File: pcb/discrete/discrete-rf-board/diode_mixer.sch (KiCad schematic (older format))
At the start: 27 parts, among them J301 Conn_Coaxial, J302 Conn_Coaxial, U302 BAT15-099R

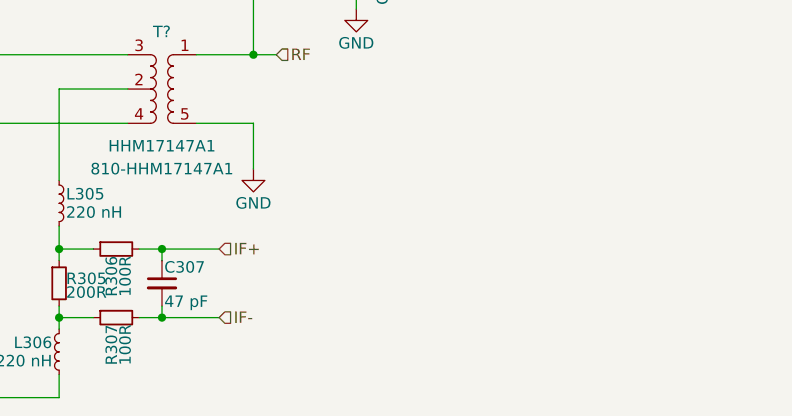
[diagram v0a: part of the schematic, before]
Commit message: Design DAC/ADC stages, pass out all control signals to top sheet
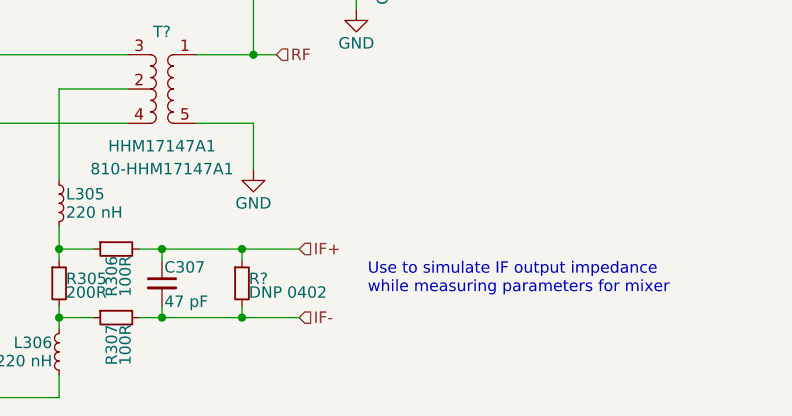
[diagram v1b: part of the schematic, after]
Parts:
- added R?: DNP 0402, symbol Device:R_Small
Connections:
- net IF+: now also R?.1
- net IF-: now also R?.2
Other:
- note added: "Use to simulate IF output impedance\nwhile measuring parameters for mixer"
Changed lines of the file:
@@
 RF
 Wire Wire Line
-	9000 4300 8750 4300
+	9350 4300 9100 4300
 Connection ~ 8750 4300
 Wire Wire Line
@@
 	8750 4600 8750 4550
 Wire Wire Line
-	9000 4600 8750 4600
+	9350 4600 9100 4600
 Connection ~ 8750 4600
-Text HLabel 9000 4300 2    50   Input ~ 0
+Text HLabel 9350 4300 2    50   Input ~ 0
 IF+
-Text HLabel 9000 4600 2    50   Input ~ 0
+Text HLabel 9350 4600 2    50   Input ~ 0
 IF-
 Wire Wire Line
@@
 Text Notes 4850 4350 0    50   ~ 0
 TODO probably add bypass cap, probably ground some part of\nthe balanced mixer to make TL design easier
+$Comp
+L Device:R_Small R?
+U 1 1 5D979A64
+P 9100 4450
+AR Path="/5CA6B0AA/5CC1CC09/5D979A64" Ref="R?"  Part="1"
+AR Path="/5CA6B0AA/5CC4015A/5D979A64" Ref="R?"  Part="1"
+F 0 "R?" H 9130 4470 50  0000 L CNN
+F 1 "DNP 0402" H 9130 4410 50  0000 L CNN
+F 2 "" H 9100 4450 50  0001 C CNN
+F 3 "~" H 9100 4450 50  0001 C CNN
+	1    9100 4450
+	1    0    0    -1
+$EndComp
+Text Notes 9650 4500 0    50   ~ 0
+Use to simulate IF output impedance\nwhile measuring parameters for mixer
+Wire Wire Line
+	9100 4350 9100 4300
+Connection ~ 9100 4300
+Wire Wire Line
+	9100 4300 8750 4300
+Wire Wire Line
+	9100 4550 9100 4600
+Connection ~ 9100 4600
+Wire Wire Line
+	9100 4600 8750 4600
 $EndSCHEMATC

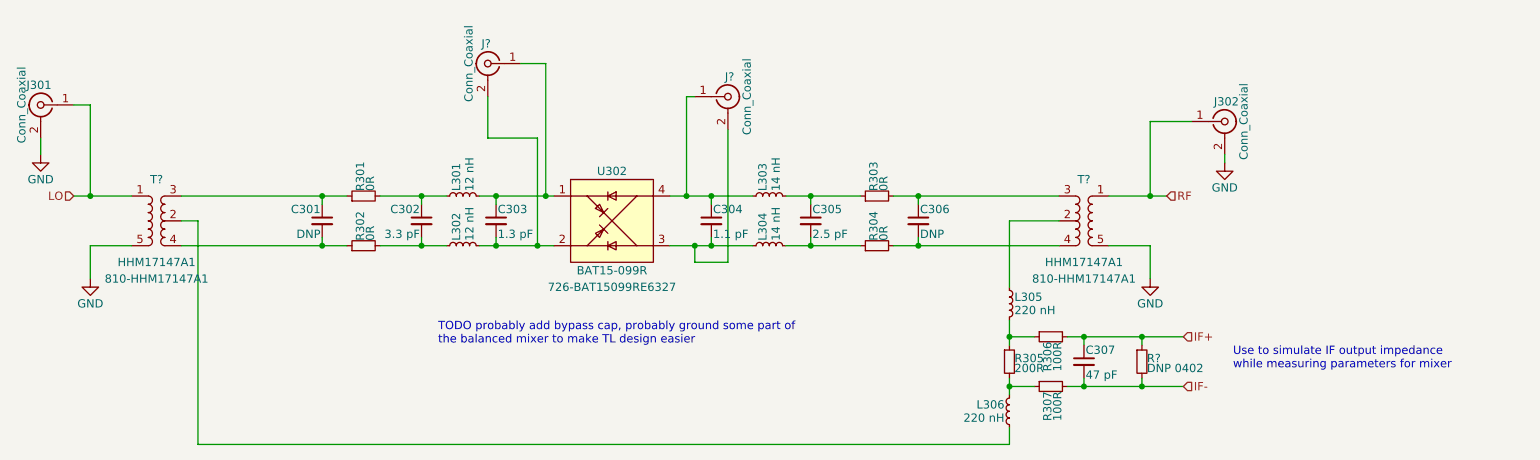
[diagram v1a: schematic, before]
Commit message: Wire out all control signals to connectors TODO PLL charge pump loop, bypass caps in attenuator circuit, antialiasing filter for ADC frontend
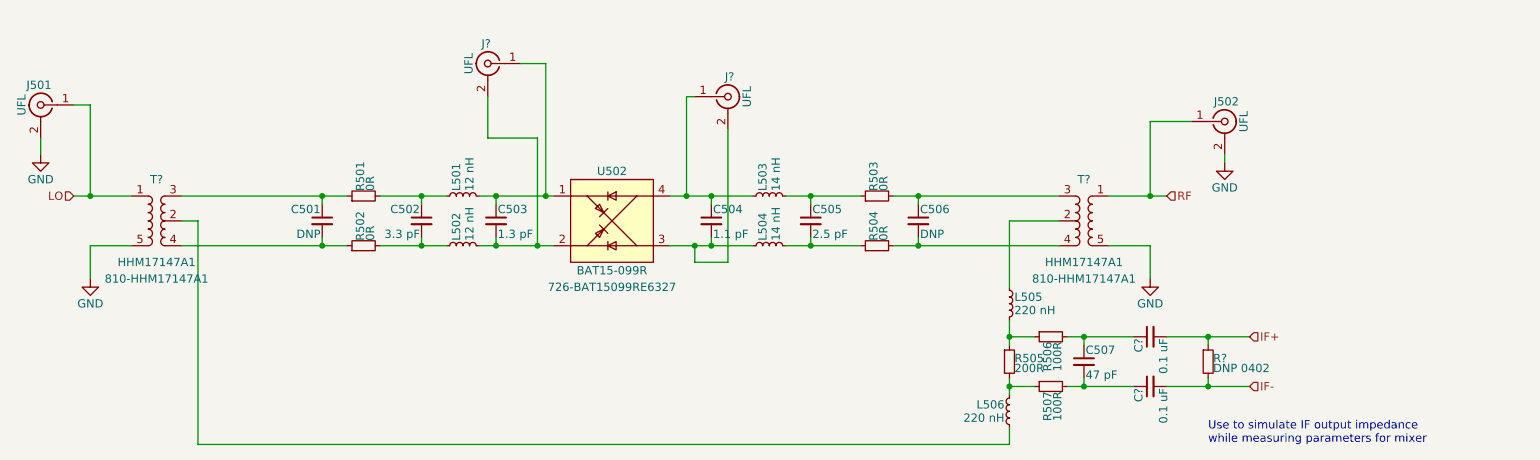
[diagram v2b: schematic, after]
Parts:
- added C? (x2): 0.1 uF, symbol Device:C_Small
- J301, J302, J? (x2): value Conn_Coaxial -> UFL
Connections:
- net IF+: now also C?.2; no longer C307.1, R306.2
- net IF-: now also C?.2; no longer C307.2, R307.2
- new net: C307.1, C?.1, R306.2
- new net: C307.2, C?.1, R307.2
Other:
- note removed: "TODO probably add bypass cap, probably ground some part of\nthe balanced mixer to make TL design easier"
- moved on the sheet: R?

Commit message: Start work in footprinting everything
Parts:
- U302: footprint (none) -> discrete_footprints:Infineon_SOT143
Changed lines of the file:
@@
 $Descr A4 11693 8268
 encoding utf-8
-Sheet 19 19
+Sheet 11 19
 Title ""
 Date ""
@@
 F 0 "U502" H 5900 3900 50  0000 C CNN
 F 1 "BAT15-099R" H 5900 3300 50  0000 C CNN
-F 2 "" H 5900 3900 50  0001 C CNN
+F 2 "discrete_footprints:Infineon_SOT143" H 5900 3900 50  0001 C CNN
 F 3 "" H 5900 3900 50  0001 C CNN
 F 4 "726-BAT15099RE6327" H 5900 3200 50  0000 C CNN "Mouser"

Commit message: The footprintening continues
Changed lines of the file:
@@
 $Descr A4 11693 8268
 encoding utf-8
-Sheet 11 19
+Sheet 19 19
 Title ""
 Date ""
@@
 AR Path="/5CA6B0AA/5CC1CC09/5CC1E322" Ref="U302"  Part="1"
 AR Path="/5CA6B0AA/5CC4015A/5CC1E322" Ref="U502"  Part="1"
-F 0 "U502" H 5900 3900 50  0000 C CNN
+F 0 "U302" H 5900 3900 50  0000 C CNN
 F 1 "BAT15-099R" H 5900 3300 50  0000 C CNN
 F 2 "discrete_footprints:Infineon_SOT143" H 5900 3900 50  0001 C CNN
@@
 AR Path="/5CA6B0AA/5CC1CC09/5CC1F89D" Ref="C304"  Part="1"
 AR Path="/5CA6B0AA/5CC4015A/5CC1F89D" Ref="C504"  Part="1"
-F 0 "C504" H 6510 3670 50  0000 L CNN
+F 0 "C304" H 6510 3670 50  0000 L CNN
 F 1 "1.1 pF" H 6510 3520 50  0000 L CNN
 F 2 "" H 6500 3600 50  0001 C CNN
@@
 AR Path="/5CA6B0AA/5CC1CC09/5CC20238" Ref="C305"  Part="1"
 AR Path="/5CA6B0AA/5CC4015A/5CC20238" Ref="C505"  Part="1"
-F 0 "C505" H 7110 3670 50  0000 L CNN
+F 0 "C305" H 7110 3670 50  0000 L CNN
 F 1 "2.5 pF" H 7110 3520 50  0000 L CNN
 F 2 "" H 7100 3600 50  0001 C CNN
@@
 AR Path="/5CA6B0AA/5CC1CC09/5CC208EE" Ref="L304"  Part="1"
 AR Path="/5CA6B0AA/5CC4015A/5CC208EE" Ref="L504"  Part="1"
-F 0 "L504" H 6880 3790 50  0000 L CNN
+F 0 "L304" H 6880 3790 50  0000 L CNN
 F 1 "14 nH" H 6880 3710 50  0000 L CNN
 F 2 "" H 6850 3750 50  0001 C CNN
@@
 AR Path="/5CA6B0AA/5CC1CC09/5CC2101C" Ref="L303"  Part="1"
 AR Path="/5CA6B0AA/5CC4015A/5CC2101C" Ref="L503"  Part="1"
-F 0 "L503" H 6880 3490 50  0000 L CNN
+F 0 "L303" H 6880 3490 50  0000 L CNN
 F 1 "14 nH" H 6880 3410 50  0000 L CNN
 F 2 "" H 6850 3450 50  0001 C CNN
@@
 AR Path="/5CA6B0AA/5CC1CC09/5CC289D9" Ref="L305"  Part="1"
 AR Path="/5CA6B0AA/5CC4015A/5CC289D9" Ref="L505"  Part="1"
-F 0 "L505" H 8330 4140 50  0000 L CNN
+F 0 "L305" H 8330 4140 50  0000 L CNN
 F 1 "220 nH" H 8330 4060 50  0000 L CNN
 F 2 "" H 8300 4100 50  0001 C CNN
@@
 AR Path="/5CA6B0AA/5CC1CC09/5CC29B4E" Ref="R305"  Part="1"
 AR Path="/5CA6B0AA/5CC4015A/5CC29B4E" Ref="R505"  Part="1"
-F 0 "R505" H 8330 4470 50  0000 L CNN
+F 0 "R305" H 8330 4470 50  0000 L CNN
 F 1 "200R" H 8330 4410 50  0000 L CNN
 F 2 "" H 8300 4450 50  0001 C CNN
@@
 AR Path="/5CA6B0AA/5CC1CC09/5CC29F9D" Ref="R306"  Part="1"
 AR Path="/5CA6B0AA/5CC4015A/5CC29F9D" Ref="R506"  Part="1"
-F 0 "R506" H 8580 4320 50  0000 L CNN
+F 0 "R306" H 8580 4320 50  0000 L CNN
 F 1 "100R" H 8580 4260 50  0000 L CNN
 F 2 "" H 8550 4300 50  0001 C CNN
@@
 AR Path="/5CA6B0AA/5CC1CC09/5CC2B0AC" Ref="C307"  Part="1"
 AR Path="/5CA6B0AA/5CC4015A/5CC2B0AC" Ref="C507"  Part="1"
-F 0 "C507" H 8760 4520 50  0000 L CNN
+F 0 "C307" H 8760 4520 50  0000 L CNN
 F 1 "47 pF" H 8760 4370 50  0000 L CNN
 F 2 "" H 8750 4450 50  0001 C CNN
@@
 AR Path="/5CA6B0AA/5CC1CC09/5CC2FA5E" Ref="#PWR0302"  Part="1"
 AR Path="/5CA6B0AA/5CC4015A/5CC2FA5E" Ref="#PWR0502"  Part="1"
-F 0 "#PWR0502" H 2750 3700 50  0001 C CNN
+F 0 "#PWR0302" H 2750 3700 50  0001 C CNN
 F 1 "GND" H 2750 3800 50  0000 C CNN
 F 2 "" H 2750 3950 50  0001 C CNN
@@
 AR Path="/5CA6B0AA/5CC1CC09/5CC3011D" Ref="#PWR0303"  Part="1"
 AR Path="/5CA6B0AA/5CC4015A/5CC3011D" Ref="#PWR0503"  Part="1"
-F 0 "#PWR0503" H 9150 3700 50  0001 C CNN
+F 0 "#PWR0303" H 9150 3700 50  0001 C CNN
 F 1 "GND" H 9150 3800 50  0000 C CNN
 F 2 "" H 9150 3950 50  0001 C CNN
@@
 AR Path="/5CA6B0AA/5CC1CC09/5CC30B27" Ref="J301"  Part="1"
 AR Path="/5CA6B0AA/5CC4015A/5CC30B27" Ref="J501"  Part="1"
-F 0 "J501" H 2460 3020 50  0000 C CNN
+F 0 "J301" H 2460 3020 50  0000 C CNN
 F 1 "UFL" V 2565 2900 50  0000 C CNN
 F 2 "" H 2450 2900 50  0001 C CNN
@@
 AR Path="/5CA6B0AA/5CC1CC09/5CC31787" Ref="J302"  Part="1"
 AR Path="/5CA6B0AA/5CC4015A/5CC31787" Ref="J502"  Part="1"
-F 0 "J502" H 9610 3120 50  0000 C CNN
+F 0 "J302" H 9610 3120 50  0000 C CNN
 F 1 "UFL" V 9715 3000 50  0000 C CNN
 F 2 "" H 9600 3000 50  0001 C CNN
@@
 AR Path="/5CA6B0AA/5CC1CC09/5CC33186" Ref="#PWR0304"  Part="1"
 AR Path="/5CA6B0AA/5CC4015A/5CC33186" Ref="#PWR0504"  Part="1"
-F 0 "#PWR0504" H 9600 3000 50  0001 C CNN
+F 0 "#PWR0304" H 9600 3000 50  0001 C CNN
 F 1 "GND" H 9600 3100 50  0000 C CNN
 F 2 "" H 9600 3250 50  0001 C CNN
@@
 AR Path="/5CA6B0AA/5CC1CC09/5CC33A73" Ref="#PWR0301"  Part="1"
 AR Path="/5CA6B0AA/5CC4015A/5CC33A73" Ref="#PWR0501"  Part="1"
-F 0 "#PWR0501" H 2450 2950 50  0001 C CNN
+F 0 "#PWR0301" H 2450 2950 50  0001 C CNN
 F 1 "GND" H 2450 3050 50  0000 C CNN
 F 2 "" H 2450 3200 50  0001 C CNN
@@
 AR Path="/5CA6B0AA/5CC1CC09/5CC5AE0B" Ref="L306"  Part="1"
 AR Path="/5CA6B0AA/5CC4015A/5CC5AE0B" Ref="L506"  Part="1"
-F 0 "L506" H 8330 4790 50  0000 L CNN
+F 0 "L306" H 8330 4790 50  0000 L CNN
 F 1 "220 nH" H 8330 4710 50  0000 L CNN
 F 2 "" H 8300 4750 50  0001 C CNN
@@
 AR Path="/5CA6B0AA/5CC1CC09/5CC5DD55" Ref="R307"  Part="1"
 AR Path="/5CA6B0AA/5CC4015A/5CC5DD55" Ref="R507"  Part="1"
-F 0 "R507" H 8580 4620 50  0000 L CNN
+F 0 "R307" H 8580 4620 50  0000 L CNN
 F 1 "100R" H 8580 4560 50  0000 L CNN
 F 2 "" H 8550 4600 50  0001 C CNN
@@
 AR Path="/5CA6B0AA/5CC1CC09/5CC22010" Ref="L302"  Part="1"
 AR Path="/5CA6B0AA/5CC4015A/5CC22010" Ref="L502"  Part="1"
-F 0 "L502" H 5030 3790 50  0000 L CNN
+F 0 "L302" H 5030 3790 50  0000 L CNN
 F 1 "12 nH" H 5030 3710 50  0000 L CNN
 F 2 "" H 5000 3750 50  0001 C CNN
@@
 AR Path="/5CA6B0AA/5CC1CC09/5CC1F7BA" Ref="C302"  Part="1"
 AR Path="/5CA6B0AA/5CC4015A/5CC1F7BA" Ref="C502"  Part="1"
-F 0 "C502" H 4760 3670 50  0000 L CNN
+F 0 "C302" H 4760 3670 50  0000 L CNN
 F 1 "3.3 pF" H 4760 3520 50  0000 L CNN
 F 2 "" H 4750 3600 50  0001 C CNN
@@
 AR Path="/5CA6B0AA/5CC1CC09/5CC1E94D" Ref="C303"  Part="1"
 AR Path="/5CA6B0AA/5CC4015A/5CC1E94D" Ref="C503"  Part="1"
-F 0 "C503" H 5210 3670 50  0000 L CNN
+F 0 "C303" H 5210 3670 50  0000 L CNN
 F 1 "1.3 pF" H 5210 3520 50  0000 L CNN
 F 2 "" H 5200 3600 50  0001 C CNN
@@
 AR Path="/5CA6B0AA/5CC1CC09/5CC22016" Ref="L301"  Part="1"
 AR Path="/5CA6B0AA/5CC4015A/5CC22016" Ref="L501"  Part="1"
-F 0 "L501" H 5030 3490 50  0000 L CNN
+F 0 "L301" H 5030 3490 50  0000 L CNN
 F 1 "12 nH" H 5030 3410 50  0000 L CNN
 F 2 "" H 5000 3450 50  0001 C CNN
@@
 AR Path="/5CA6B0AA/5CC1CC09/5D51EF09" Ref="C301"  Part="1"
 AR Path="/5CA6B0AA/5CC4015A/5D51EF09" Ref="C501"  Part="1"
-F 0 "C501" H 4160 3670 50  0000 L CNN
+F 0 "C301" H 4160 3670 50  0000 L CNN
 F 1 "DNP" H 4160 3520 50  0000 L CNN
 F 2 "" H 4150 3600 50  0001 C CNN
@@
 AR Path="/5CA6B0AA/5CC1CC09/5D51FC82" Ref="R301"  Part="1"
 AR Path="/5CA6B0AA/5CC4015A/5D51FC82" Ref="R501"  Part="1"
-F 0 "R501" H 4430 3470 50  0000 L CNN
+F 0 "R301" H 4430 3470 50  0000 L CNN
 F 1 "0R" H 4430 3410 50  0000 L CNN
 F 2 "" H 4400 3450 50  0001 C CNN
@@
 AR Path="/5CA6B0AA/5CC1CC09/5D5221DB" Ref="R302"  Part="1"
 AR Path="/5CA6B0AA/5CC4015A/5D5221DB" Ref="R502"  Part="1"
-F 0 "R502" H 4430 3770 50  0000 L CNN
+F 0 "R302" H 4430 3770 50  0000 L CNN
 F 1 "0R" H 4430 3710 50  0000 L CNN
 F 2 "" H 4400 3750 50  0001 C CNN
@@
 AR Path="/5CA6B0AA/5CC1CC09/5D52D7BD" Ref="C306"  Part="1"
 AR Path="/5CA6B0AA/5CC4015A/5D52D7BD" Ref="C506"  Part="1"
-F 0 "C506" H 7760 3670 50  0000 L CNN
+F 0 "C306" H 7760 3670 50  0000 L CNN
 F 1 "DNP" H 7760 3520 50  0000 L CNN
 F 2 "" H 7750 3600 50  0001 C CNN
@@
 AR Path="/5CA6B0AA/5CC1CC09/5D52D7C3" Ref="R303"  Part="1"
 AR Path="/5CA6B0AA/5CC4015A/5D52D7C3" Ref="R503"  Part="1"
-F 0 "R503" H 7530 3470 50  0000 L CNN
+F 0 "R303" H 7530 3470 50  0000 L CNN
 F 1 "0R" H 7530 3410 50  0000 L CNN
 F 2 "" H 7500 3450 50  0001 C CNN
@@
 AR Path="/5CA6B0AA/5CC1CC09/5D52D7C9" Ref="R304"  Part="1"
 AR Path="/5CA6B0AA/5CC4015A/5D52D7C9" Ref="R504"  Part="1"
-F 0 "R504" H 7530 3770 50  0000 L CNN
+F 0 "R304" H 7530 3770 50  0000 L CNN
 F 1 "0R" H 7530 3710 50  0000 L CNN
 F 2 "" H 7500 3750 50  0001 C CNN

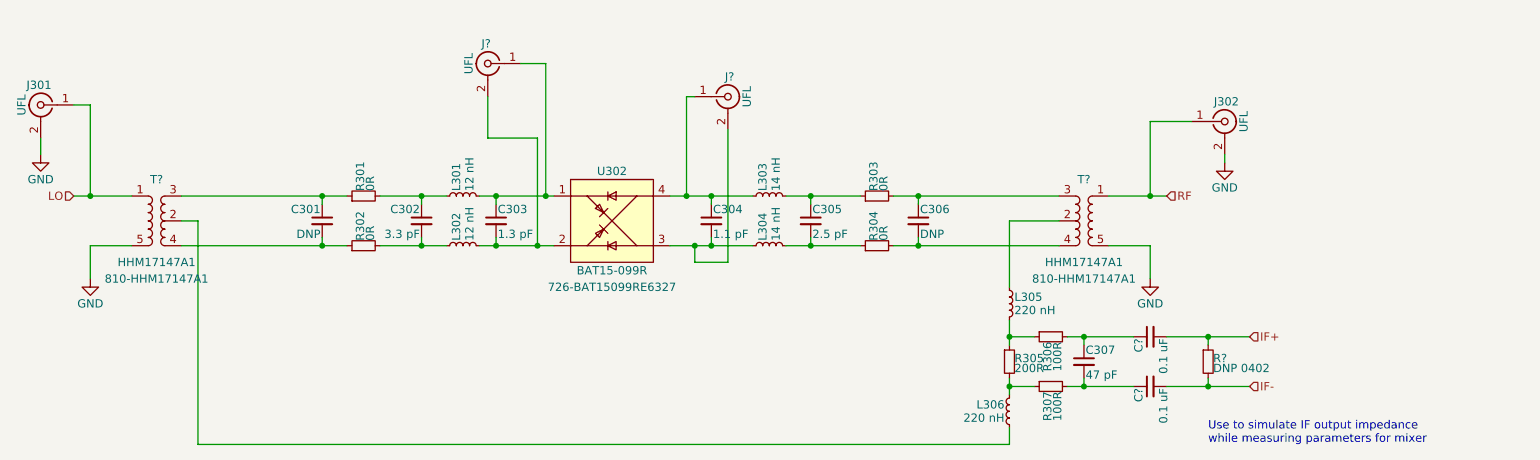
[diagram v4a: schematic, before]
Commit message: Add matching PNP/NPN transistor pairs, fix pin numbering for BFU520R transistors TODO fix biasing on power stage, source last NPN transistor, autofill and start sourcing passives
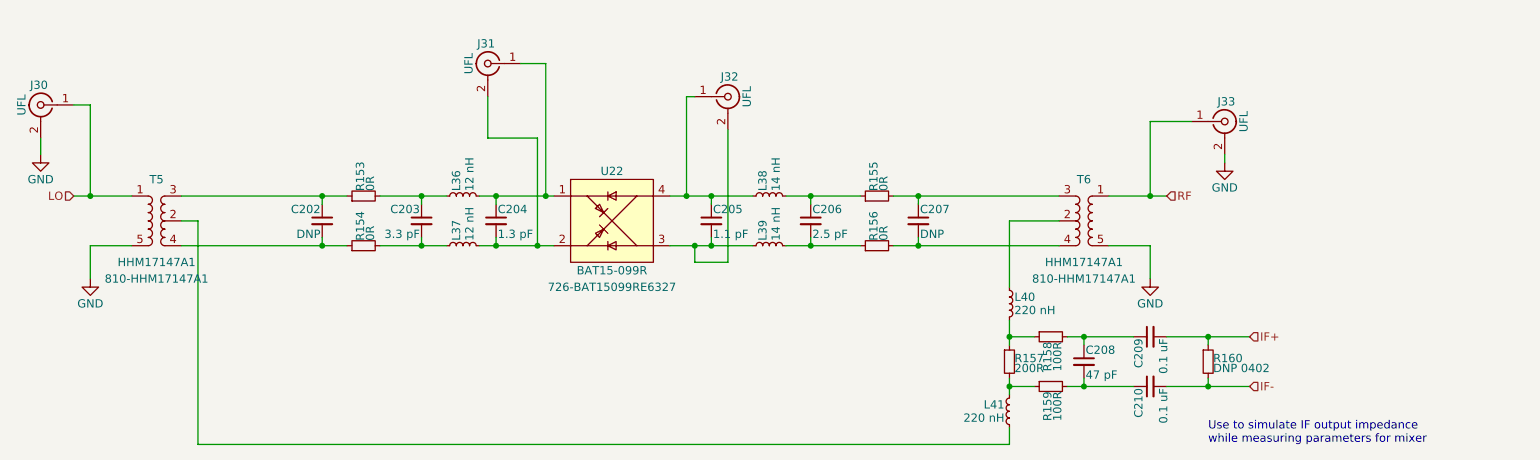
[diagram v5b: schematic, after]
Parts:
- gave numbers to parts that had none: 7
- renumbered C301 to C202, C302 to C203, C303 to C204, C304 to C205, C305 to C206, C306 to C207, C307 to C208, J301 to J30, J302 to J33, L301 to L36, L302 to L37, L303 to L38, L304 to L39, L305 to L40, L306 to L41, R301 to R153, R302 to R154, R303 to R155, R304 to R156, R305 to R157, R306 to R158, R307 to R159, U302 to U22
